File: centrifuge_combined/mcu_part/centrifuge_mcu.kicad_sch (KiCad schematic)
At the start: 16 parts, among them J506 DDCI2C2, J516 Conn_02x06_Odd_Even, J517 DDCI2C1

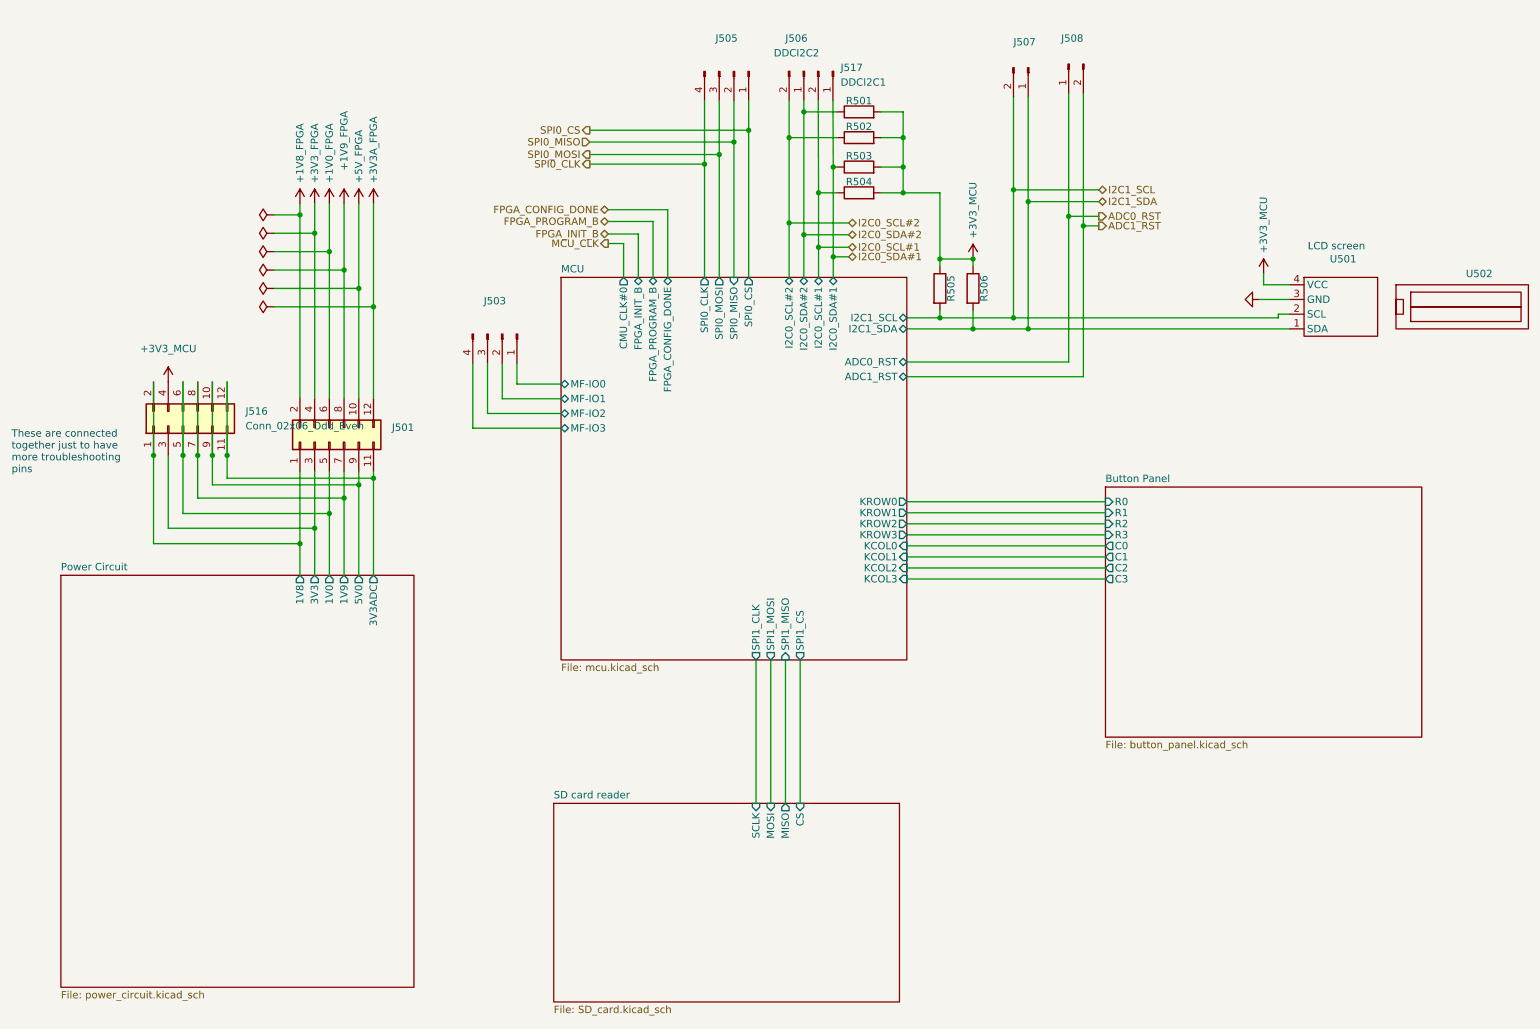
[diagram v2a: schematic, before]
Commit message: fixed keypad hole sizes, and submitted
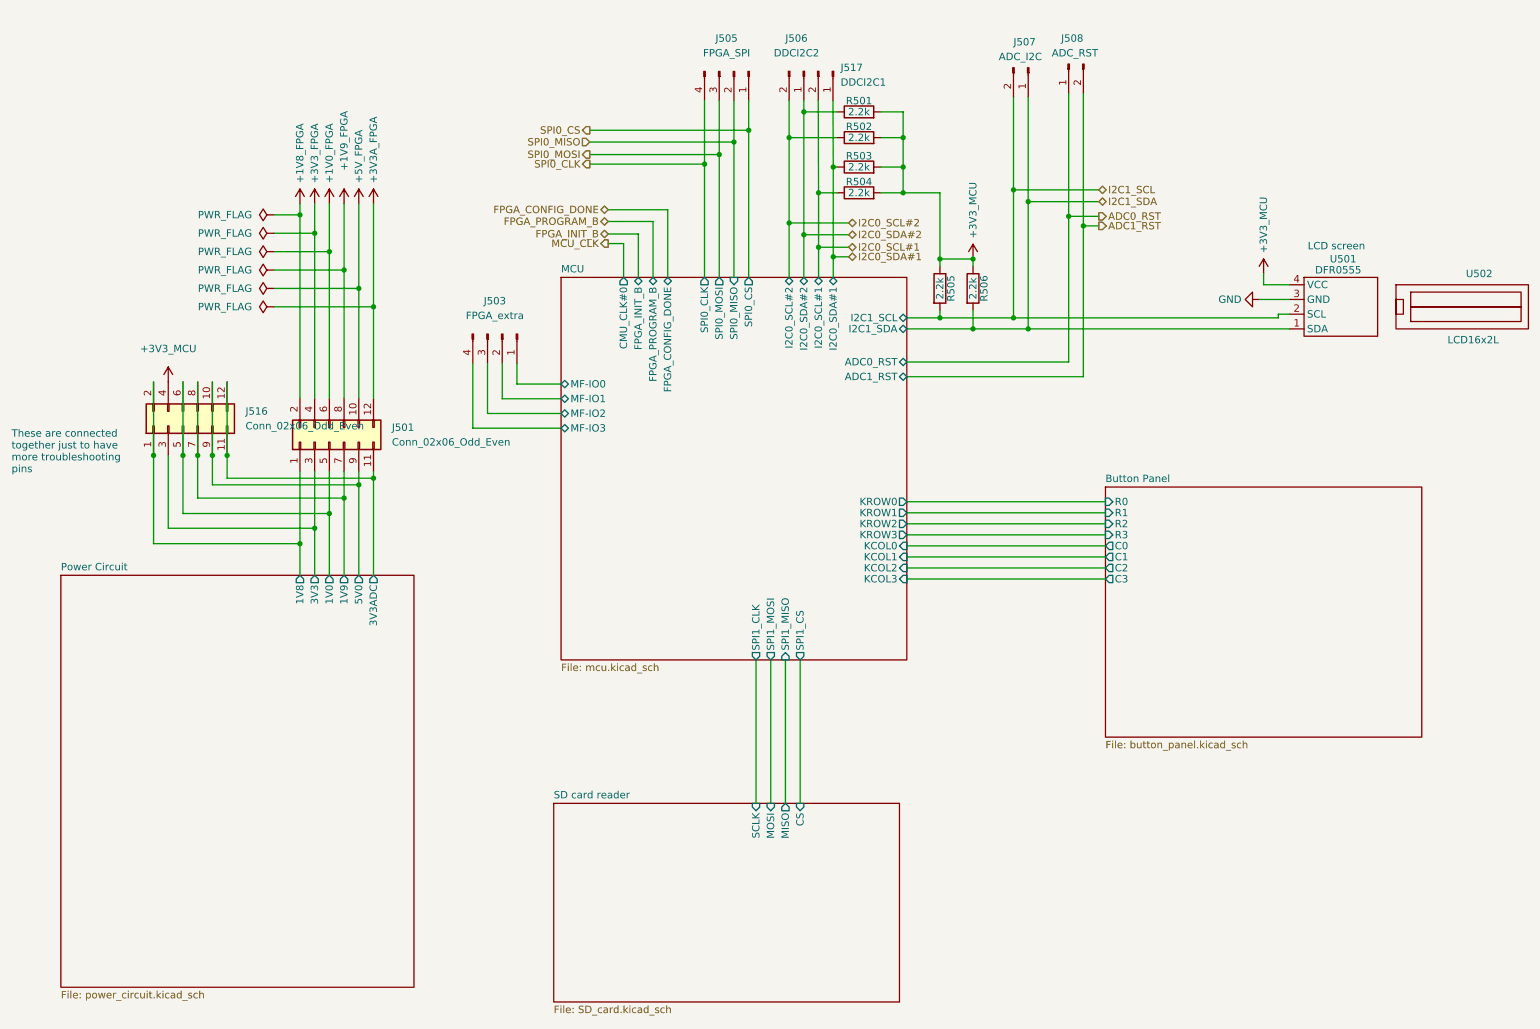
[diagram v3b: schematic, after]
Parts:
- J501: value (none) -> Conn_02x06_Odd_Even
- J503: value (none) -> FPGA_extra
- J505: value (none) -> FPGA_SPI
- J507: value (none) -> ADC_I2C
- J508: value (none) -> ADC_RST
- R501, R502, R503, R504, R505, R506: value (none) -> 2.2k
- U501: value (none) -> DFR0555
- U502: value (none) -> LCD16x2L
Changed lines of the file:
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@@
       (effects (font (size 1.27 1.27)) hide)
     )
-    (property "Value" "" (id 1) (at 55.88 53.9749 90)
+    (property "Value" "PWR_FLAG" (id 1) (at 55.88 53.9749 90)
       (effects (font (size 1.27 1.27)) (justify left))
     )
@@
     (in_bom yes) (on_board yes)
     (property "Reference" "R503" (id 0) (at 160.655 40.64 90))
-    (property "Value" "" (id 1) (at 160.655 42.545 90))
+    (property "Value" "2.2k" (id 1) (at 160.655 42.545 90))
     (property "Footprint" "" (id 2) (at 160.655 44.323 90)
       (effects (font (size 1.27 1.27)) hide)
@@
     (in_bom yes) (on_board yes) (fields_autoplaced)
     (property "Reference" "J505" (id 0) (at 137.795 20.32 90))
-    (property "Value" "" (id 1) (at 137.795 22.86 90))
+    (property "Value" "FPGA_SPI" (id 1) (at 137.795 22.86 90))
     (property "Footprint" "" (id 2) (at 139.065 26.035 0)
       (effects (font (size 1.27 1.27)) hide)
@@
     (in_bom yes) (on_board yes)
     (property "Reference" "R505" (id 0) (at 176.53 63.5 90))
-    (property "Value" "" (id 1) (at 174.625 63.5 90))
+    (property "Value" "2.2k" (id 1) (at 174.625 63.5 90))
     (property "Footprint" "" (id 2) (at 172.847 63.5 90)
       (effects (font (size 1.27 1.27)) hide)
@@
     (in_bom yes) (on_board yes)
     (property "Reference" "R506" (id 0) (at 182.245 63.5 90))
-    (property "Value" "" (id 1) (at 180.34 63.5 90))
+    (property "Value" "2.2k" (id 1) (at 180.34 63.5 90))
     (property "Footprint" "" (id 2) (at 178.562 63.5 90)
       (effects (font (size 1.27 1.27)) hide)
@@
       (effects (font (size 1.27 1.27)) hide)
     )
-    (property "Value" "" (id 1) (at 55.88 66.6749 90)
+    (property "Value" "PWR_FLAG" (id 1) (at 55.88 66.6749 90)
       (effects (font (size 1.27 1.27)) (justify left))
     )
@@
     (in_bom yes) (on_board yes)
     (property "Reference" "R504" (id 0) (at 160.655 45.085 90))
-    (property "Value" "" (id 1) (at 160.655 46.99 90))
+    (property "Value" "2.2k" (id 1) (at 160.655 46.99 90))
     (property "Footprint" "" (id 2) (at 160.655 48.768 90)
       (effects (font (size 1.27 1.27)) hide)
@@
       (effects (font (size 1.27 1.27)) hide)
     )
-    (property "Value" "" (id 1) (at 55.88 63.4999 90)
+    (property "Value" "PWR_FLAG" (id 1) (at 55.88 63.4999 90)
       (effects (font (size 1.27 1.27)) (justify left))
     )
@@
       (effects (font (size 1.27 1.27)) (justify left))
     )
-    (property "Value" "" (id 1) (at 262.255 72.39 0)
+    (property "Value" "LCD16x2L" (id 1) (at 262.255 72.39 0)
       (effects (font (size 1.27 1.27)) (justify left))
     )
@@
       (effects (font (size 1.27 1.27)) hide)
     )
-    (property "Value" "" (id 1) (at 55.88 60.3249 90)
+    (property "Value" "PWR_FLAG" (id 1) (at 55.88 60.3249 90)
       (effects (font (size 1.27 1.27)) (justify left))
     )
@@
     (in_bom yes) (on_board yes) (fields_autoplaced)
     (property "Reference" "J503" (id 0) (at 97.79 65.659 90))
-    (property "Value" "" (id 1) (at 97.79 68.199 90))
+    (property "Value" "FPGA_extra" (id 1) (at 97.79 68.199 90))
     (property "Footprint" "" (id 2) (at 99.06 71.374 0)
       (effects (font (size 1.27 1.27)) hide)
@@
       (effects (font (size 1.27 1.27)) (justify left))
     )
-    (property "Value" "" (id 1) (at 239.395 60.325 0)
+    (property "Value" "DFR0555" (id 1) (at 239.395 60.325 0)
       (effects (font (size 1.27 1.27)) (justify left))
     )
@@
       (effects (font (size 1.27 1.27)) (justify left))
     )
-    (property "Value" "" (id 1) (at 184.785 23.495 90)
+    (property "Value" "ADC_I2C" (id 1) (at 184.785 23.495 90)
       (effects (font (size 1.27 1.27)) (justify left))
     )
@@
       (effects (font (size 1.27 1.27)) hide)
     )
-    (property "Value" "" (id 1) (at 55.88 57.1499 90)
+    (property "Value" "PWR_FLAG" (id 1) (at 55.88 57.1499 90)
       (effects (font (size 1.27 1.27)) (justify left))
     )
@@
       (effects (font (size 1.27 1.27)) hide)
     )
-    (property "Value" "" (id 1) (at 55.88 50.7999 90)
+    (property "Value" "PWR_FLAG" (id 1) (at 55.88 50.7999 90)
       (effects (font (size 1.27 1.27)) (justify left))
     )
@@
       (effects (font (size 1.27 1.27)) hide)
     )
-    (property "Value" "" (id 1) (at 226.695 65.4049 90)
+    (property "Value" "GND" (id 1) (at 226.695 65.4049 90)
       (effects (font (size 1.27 1.27)) (justify right))
     )
@@
       (effects (font (size 1.27 1.27)) (justify right))
     )
-    (property "Value" "" (id 1) (at 80.01 90.0429 90)
+    (property "Value" "Conn_02x06_Odd_Even" (id 1) (at 80.01 90.0429 90)
       (effects (font (size 1.27 1.27)) (justify right))
     )
@@
       (effects (font (size 1.27 1.27)) (justify left))
     )
-    (property "Value" "" (id 1) (at 201.93 22.86 90)
+    (property "Value" "ADC_RST" (id 1) (at 201.93 22.86 90)
       (effects (font (size 1.27 1.27)) (justify left))
     )
@@
     (in_bom yes) (on_board yes)
     (property "Reference" "R501" (id 0) (at 160.655 31.115 90))
-    (property "Value" "" (id 1) (at 160.655 33.02 90))
+    (property "Value" "2.2k" (id 1) (at 160.655 33.02 90))
     (property "Footprint" "" (id 2) (at 160.655 34.798 90)
       (effects (font (size 1.27 1.27)) hide)
@@
     (in_bom yes) (on_board yes)
     (property "Reference" "R502" (id 0) (at 160.655 35.56 90))
-    (property "Value" "" (id 1) (at 160.655 37.465 90))
+    (property "Value" "2.2k" (id 1) (at 160.655 37.465 90))
     (property "Footprint" "" (id 2) (at 160.655 39.243 90)
       (effects (font (size 1.27 1.27)) hide)
